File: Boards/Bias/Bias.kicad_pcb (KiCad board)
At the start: 2 copper layers, 80 x 50 mm, 40 parts, among them P1 CONN_12V, P2 CONN_R, U1 LM339

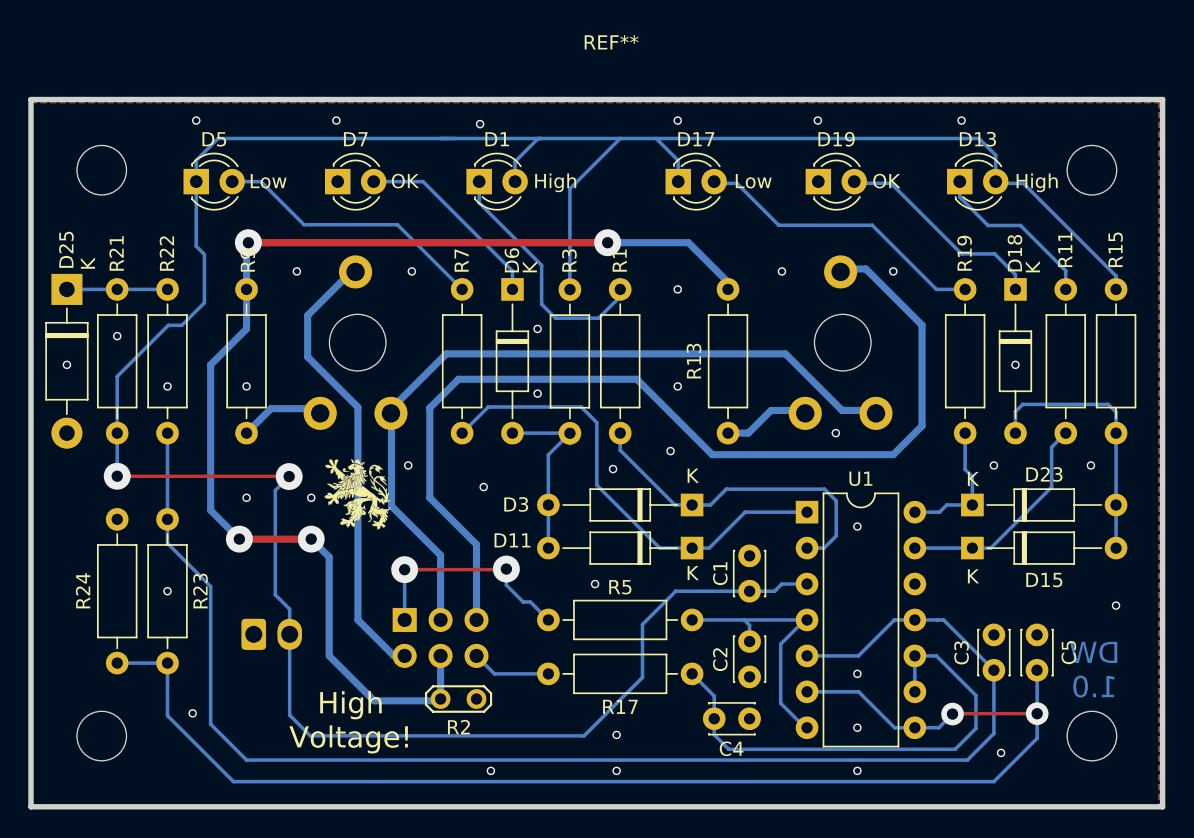
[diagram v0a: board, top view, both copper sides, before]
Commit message: Added Mounting holes, Moved -60V Divider to HV Board, eliminated +450V Connector and Feedback Connector on Amp Board
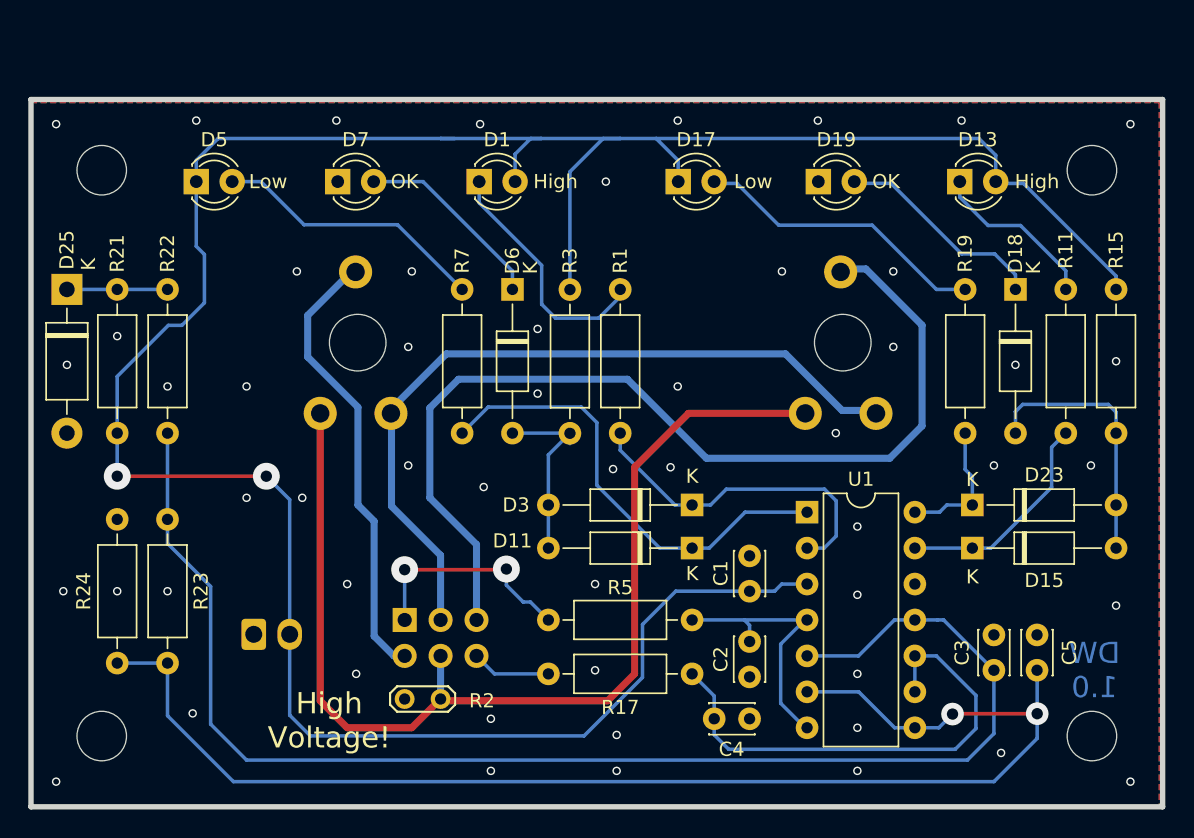
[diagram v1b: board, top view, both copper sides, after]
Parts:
- removed G***: LOGO, Loewe:Loewe_Klein
- removed R13, R9: 10k, Resistor_THT:R_Axial_DIN0207_L6.3mm_D2.5mm_P10.16mm_Horizontal
- turned R2 to 180 degrees
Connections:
- RV1 pad 1: Net-(R9-Pad1) -> GNDS
- RV3 pad 1: Net-(R13-Pad1) -> GNDS
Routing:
- net GNDS: track 84.6 -> 76.7 mm, vias 4 -> 0
- net Net-(R13-Pad1): track 6.02 -> 0.00 mm
- net Net-(R9-Pad1): track 5.96 -> 0.00 mm
- net +12V: track 192.6 -> 191.9 mm
- net GND: vias 40 -> 54
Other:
- board text added: "12V"
- board text added: "Amp"

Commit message: 6,3V und 12V auf einer Platine zusammengefasst
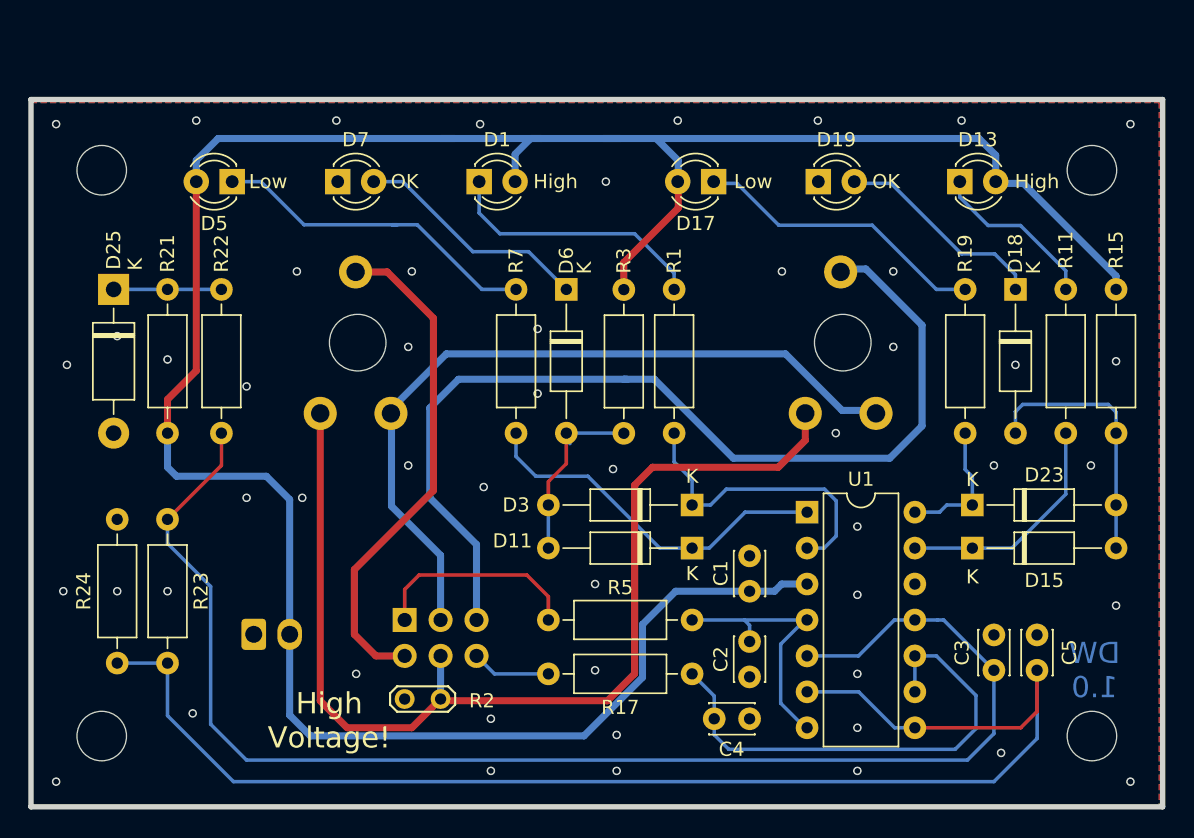
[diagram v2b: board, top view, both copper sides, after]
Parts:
- moved D6 3.81 mm to (178.1, 75.7)
- moved R1 3.81 mm to (185.7, 75.7)
- moved R3 3.81 mm to (182.1, 75.7)
- moved R7 3.81 mm to (174.5, 75.7)
- moved R22 3.81 mm to (153.7, 75.7)
- moved R21 3.56 mm to (149.9, 85.9)
- moved D25 3.30 mm to (146.1, 75.7)
- moved D5 2.54 mm to (154.4, 68.1), turned to 180 degrees
- moved D17 2.51 mm to (188.5, 68.1), turned to 180 degrees
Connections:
- D17 pad 1: +12V -> Net-(D17-Pad1)
- D17 pad 2: Net-(D17-Pad2) -> +12V
- D5 pad 1: +12V -> Net-(D5-Pad1)
- D5 pad 2: Net-(D5-Pad2) -> +12V
- R19 pad 1: Net-(D17-Pad2) -> Net-(D17-Pad1)
- R7 pad 1: Net-(D5-Pad2) -> Net-(D5-Pad1)
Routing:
- net Net-(D5-Pad1): track 0.00 -> 23.6 mm
- net Net-(D17-Pad1): track 0.00 -> 20.9 mm
- net Net-(D17-Pad2): track 20.9 -> 0.00 mm
- net Net-(D5-Pad2): track 19.4 -> 0.00 mm
- net +12V: track 191.9 -> 183.4 mm, vias 2 -> 0
- net Net-(D11-Pad1): track 33.6 -> 26.7 mm
- net /UG_R1: track 32.2 -> 35.7 mm
- net Net-(D6-Pad1): track 13.7 -> 16.8 mm
- net REF_L: track 94.5 -> 97.5 mm, vias 2 -> 0
- net Net-(D3-Pad1): track 23.9 -> 21.5 mm
- net REF_H: track 99.2 -> 100.8 mm
- net Net-(D1-Pad1): track 17.6 -> 18.9 mm
- net Net-(D15-Pad1): track 15.7 -> 16.6 mm
- net /BIAS_R1: track 15.9 -> 15.0 mm, vias 2 -> 0
- net Net-(D25-Pad1): track 7.11 -> 7.62 mm
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
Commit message: Reworked Delay + Layout changed
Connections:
- P1 pad 1: GND -> +12V
- P1 pad 2: +12V -> GND
- P2 pad 1: /BIAS_R1 -> /UG_R1
- P2 pad 2: /UG_R1 -> /BIAS_R1
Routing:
- net /BIAS_R1: track 15.0 -> 20.8 mm, vias 0 -> 1
- net /UG_R1: track 35.7 -> 30.7 mm
- net /UG_R2: track 70.2 -> 67.8 mm
- net +12V: track 183.4 -> 181.9 mm
- net Net-(D6-Pad1): track 16.8 -> 17.5 mm
- net GND: track 0.00 -> 0.06 mm, vias 51 -> 55

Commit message: Work in progess - many LAyour changes
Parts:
- removed P1: CONN_12V, Connector_Molex:Molex_KK-254_AE-6410-02A_1x02_P2.54mm_Vertical
- removed P2: CONN_R, Connector_PinHeader_2.54mm:PinHeader_2x03_P2.54mm_Vertical
- removed R2: 0R, TestPoint:TestPoint_2Pads_Pitch2.54mm_Drill0.8mm
- added J1: Conn_01x08, Connector_PinHeader_2.54mm:PinHeader_2x04_P2.54mm_Vertical, B.Cu at (160.7, 95.9)
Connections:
- RV1 pad 1: GNDS -> GND
- RV3 pad 1: GNDS -> GND
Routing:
- net GNDS: track 77.1 -> 0.00 mm
- net /BIAS_R2: track 5.61 -> 14.7 mm
- net +12V: track 181.9 -> 175.5 mm
- net /UG_R1: track 30.7 -> 25.1 mm
- net -60V: track 53.7 -> 49.7 mm
- net /UG_R2: track 67.8 -> 64.4 mm
- net /BIAS_R1: track 20.8 -> 20.0 mm, vias 1 -> 0
- net GND: track 0.06 -> 0.00 mm, vias 55 -> 60
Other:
- board text removed: "12V"

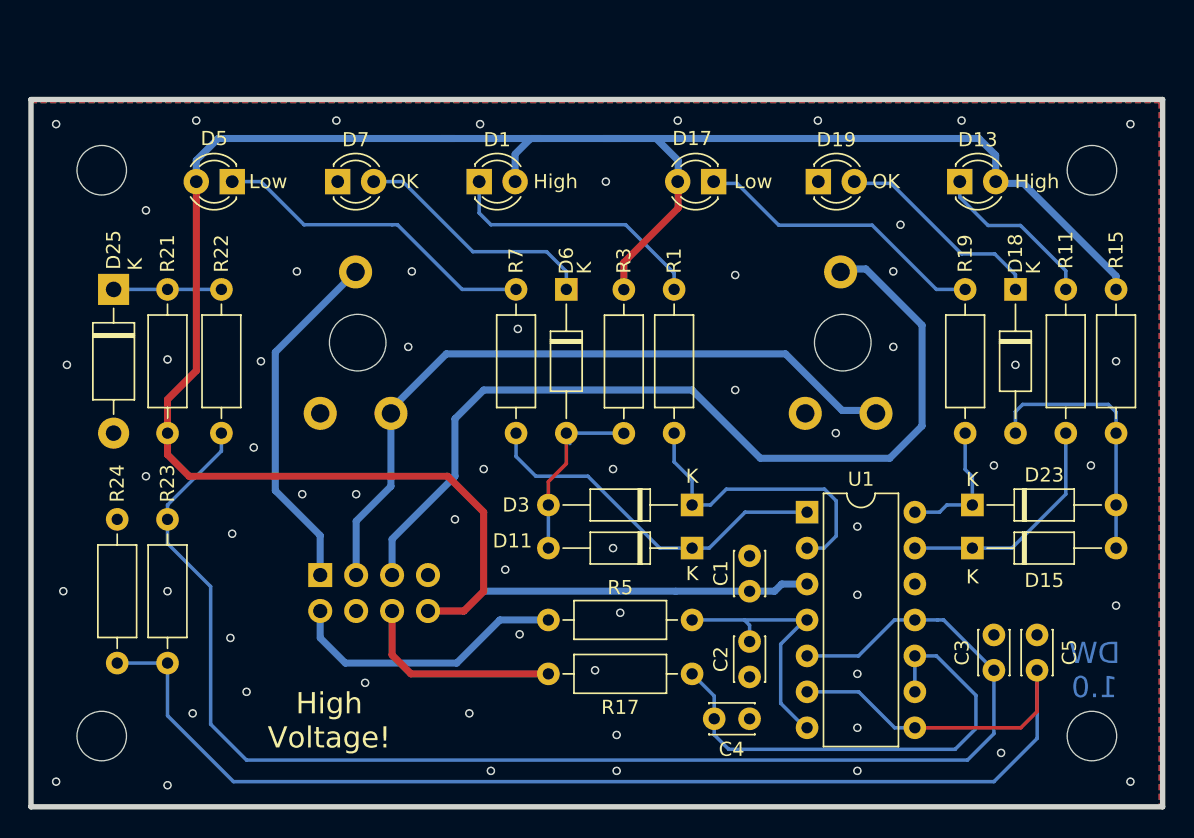
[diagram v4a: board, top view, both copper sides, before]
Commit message: 6.3V, 400V und 400V Regler Boards bestellt
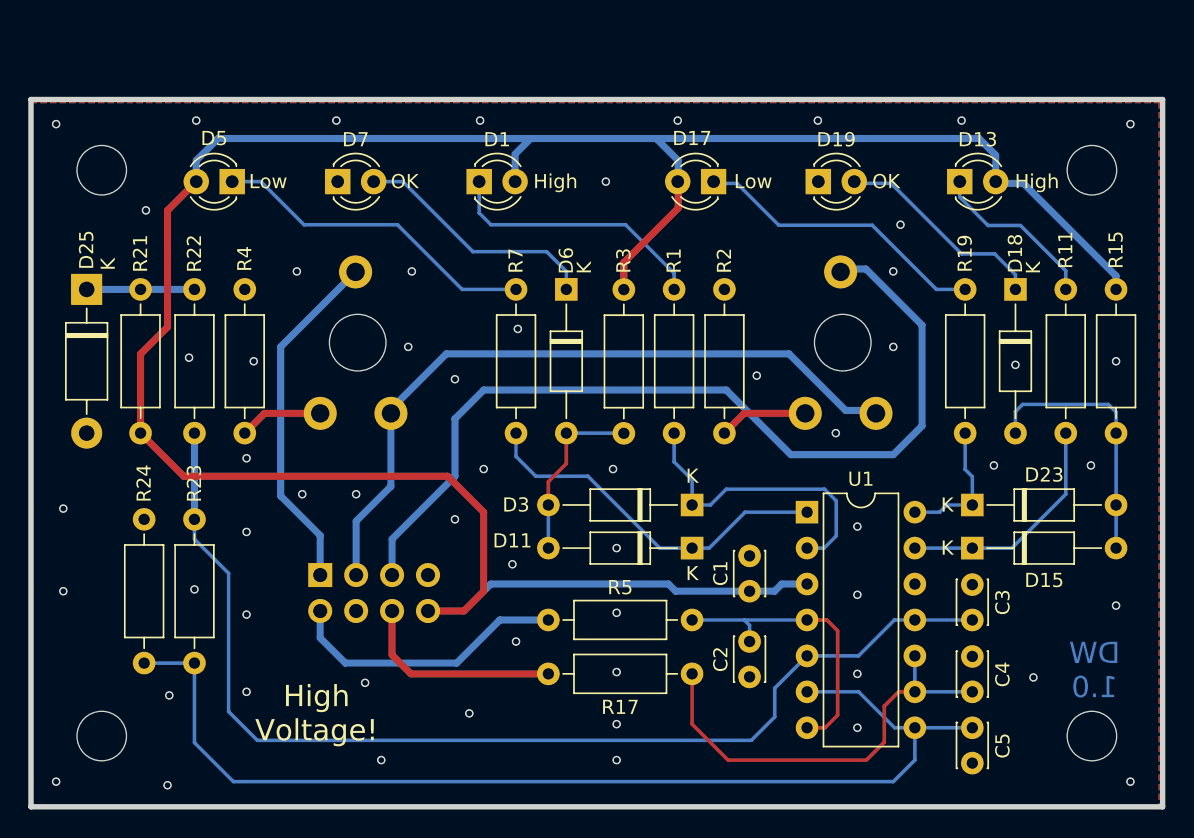
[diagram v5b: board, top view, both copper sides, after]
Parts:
- added R2: 10k, Resistor_THT:R_Axial_DIN0207_L6.3mm_D2.5mm_P10.16mm_Horizontal, F.Cu at (189.2, 85.9)
- added R4: 10k, Resistor_THT:R_Axial_DIN0207_L6.3mm_D2.5mm_P10.16mm_Horizontal, F.Cu at (155.3, 85.9)
- moved C4 18.3 mm to (206.8, 104.1), turned to 90 degrees
- moved C5 6.12 mm to (206.8, 106.7), turned to -90 degrees
- moved C3 3.87 mm to (206.8, 99.1)
- moved D25 1.91 mm to (144.1, 75.7)
- moved R21 1.91 mm to (148.0, 85.9)
- moved R22 1.91 mm to (151.8, 75.7)
- moved R24 1.91 mm to (148.2, 102.1)
- moved R23 1.90 mm to (151.8, 91.9)
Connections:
- RV1 pad 1: GND -> Net-(R4-Pad1)
- RV3 pad 1: GND -> Net-(R2-Pad1)
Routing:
- net REF_H: track 100.8 -> 78.8 mm
- net REF_L: track 97.5 -> 76.9 mm
- net Net-(R2-Pad1): track 0.00 -> 6.29 mm
- net Net-(R4-Pad1): track 0.00 -> 5.91 mm
- net Net-(U1C--): track 34.8 -> 30.4 mm
- net +12V: track 175.5 -> 173.8 mm
- net Net-(U1A--): track 19.1 -> 20.8 mm
- net Net-(D11-A): track 13.5 -> 12.7 mm
- net Net-(D11-K): track 26.7 -> 26.0 mm
- net GND: vias 60 -> 58
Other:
- net class Default removed

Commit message: Leiterplatte erstellt
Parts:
- added G***: LOGO, Loewe:Loewe_Klein, F.Cu at (156.5, 94.0)
- C1, C2, C3, C4, C5: footprint Capacitor_THT:C_Disc_D3.0mm_W2.0mm_P2.50mm -> Capacitor_THT:C_Disc_D4.3mm_W1.9mm_P5.00mm
- J1: footprint Connector_PinHeader_2.54mm:PinHeader_2x04_P2.54mm_Vertical -> Connector_IDC:IDC-Header_2x04_P2.54mm_Vertical
- moved D11 3.05 mm to (186.9, 90.9)
- moved D3 3.05 mm to (186.9, 94.0)
- moved D13 2.64 mm to (208.5, 68.1), turned to 180 degrees
- moved C4 2.59 mm to (206.2, 101.6), turned to 0 degrees
- moved D1 2.58 mm to (174.5, 68.1), turned to 180 degrees
- moved C5 2.34 mm to (206.2, 104.4), turned to 0 degrees
- moved C2 1.61 mm to (191.5, 99.1)
- moved C1 0.72 mm to (191.5, 96.5)
- moved RV3 0.68 mm to (194.7, 85.1)
- moved RV1 0.62 mm to (160.7, 85.1)
- moved C3 0.57 mm to (206.2, 98.8), turned to 0 degrees
- moved D15 0.51 mm to (206.2, 94.0)
- moved D23 0.51 mm to (206.2, 90.9)
- moved R11 0.51 mm to (212.9, 75.7)
- moved R15 0.51 mm to (216.4, 75.7)
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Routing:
- net /UG_R2: track 64.2 -> 43.9 mm
- net REF_L: track 76.9 -> 70.8 mm
- net Net-(D1-K): track 18.9 -> 15.0 mm
- net +12V: track 173.8 -> 177.1 mm
- net Net-(D3-K): track 21.5 -> 18.9 mm
- net Net-(D13-K): track 11.9 -> 9.42 mm
- net Net-(D11-K): track 26.0 -> 28.1 mm
- net -60V: track 49.7 -> 47.7 mm
- net Net-(U1A--): track 20.8 -> 19.1 mm
- net /UG_R1: track 24.8 -> 23.8 mm
- net Net-(D23-K): track 9.56 -> 8.85 mm
- net Net-(D15-A): track 18.2 -> 18.9 mm
- net GND: vias 58 -> 62
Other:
- rule pad_to_mask_clearance: 0.2 -> 0
